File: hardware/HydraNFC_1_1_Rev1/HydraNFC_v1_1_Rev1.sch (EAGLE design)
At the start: 46 parts, among them IC1 TRF7970ARHB-32, J1 HYDRABUS_SHIELD_CON_HEADER_2X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, J2 HYDRABUS_SHIELD_CON_HEADER_2X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, J3 HYDRABUS_SHIELD_CON_HEADER_2X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, K1 BUTTON-4P-3100010P1, K2 BUTTON-4P-3100010P1, K3 BUTTON-2P-REINFORCE-3100060P1, K4 BUTTON-2P-REINFORCE-3100060P1, X1 SMA-142-0701-801/806

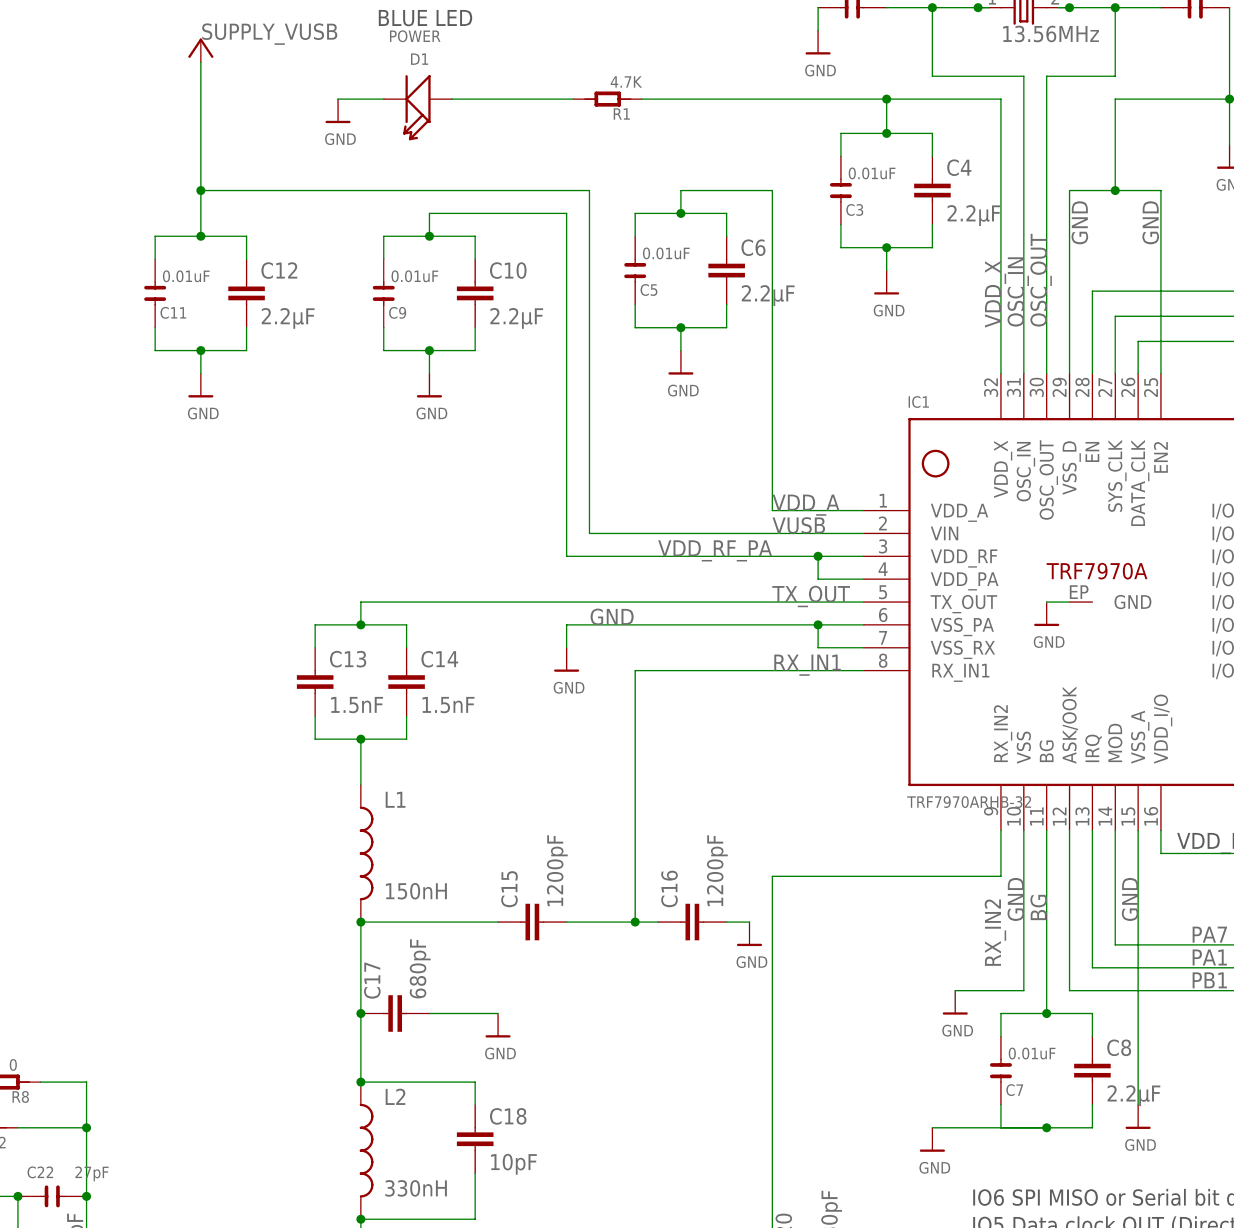
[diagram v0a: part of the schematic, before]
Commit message: Fixed Typo in Schematic/BOM Description for Decoupling Capacitor C3 & C5 & C7 & C9 & C11 which are 100nF (wrong value was 0.01uF so 10nF)
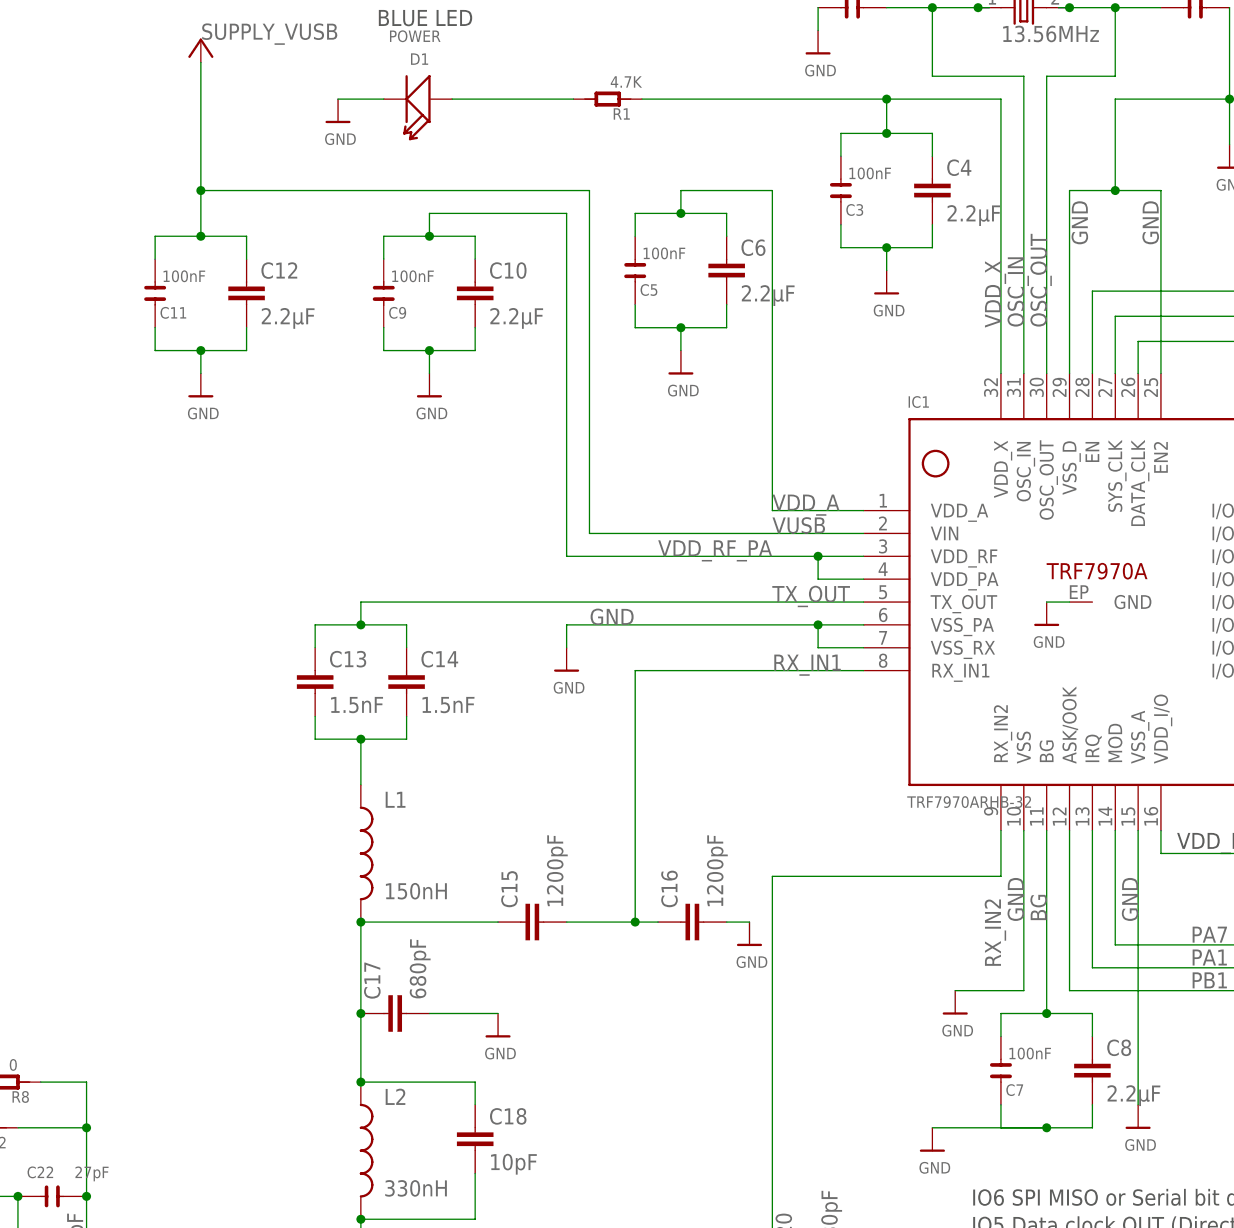
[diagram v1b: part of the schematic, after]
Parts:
- C11, C3, C5, C7, C9: value 0.01uF -> 100nF
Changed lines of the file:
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@@
 <?xml version="1.0" encoding="utf-8"?>
 <!DOCTYPE eagle SYSTEM "eagle.dtd">
-<eagle version="6.5.0">
+<eagle version="7.1.0">
 <drawing>
 <settings>
@@
 </part>
 <part name="VUSB1" library="dp_devices" deviceset="SUPPLY_VUSB" device=""/>
-<part name="C7" library="OPL" deviceset="C*" device="-0603" value="0.01uF">
+<part name="C7" library="OPL" deviceset="C*" device="-0603" value="100nF">
 <attribute name="OPL" value="0100020P1"/>
 </part>
 <part name="+3V1" library="supply1" deviceset="+3V3" device=""/>
-<part name="C3" library="OPL" deviceset="C*" device="-0603" value="0.01uF">
-<attribute name="OPL" value="0100020P1"/>
-</part>
-<part name="C5" library="OPL" deviceset="C*" device="-0603" value="0.01uF">
-<attribute name="OPL" value="0100020P1"/>
-</part>
-<part name="C9" library="OPL" deviceset="C*" device="-0603" value="0.01uF">
-<attribute name="OPL" value="0100020P1"/>
-</part>
-<part name="C11" library="OPL" deviceset="C*" device="-0603" value="0.01uF">
-<attribute name="OPL" value="0100020P1"/>
-</part>
+<part name="C3" library="OPL" deviceset="C*" device="-0603" value="100nF">
+<attribute name="OPL" value="0100020P1"/>
+</part>
+<part name="C5" library="OPL" deviceset="C*" device="-0603" value="100nF">
+<attribute name="OPL" value="0100020P1"/>
+</part>
+<part name="C9" library="OPL" deviceset="C*" device="-0603" value="100nF">
+<attribute name="OPL" value="0100020P1"/>
+</part>
+<part name="C11" library="OPL" deviceset="C*" device="-0603" value="100nF">
+<attribute name="OPL" value="0100020P1"/>
+</part>
